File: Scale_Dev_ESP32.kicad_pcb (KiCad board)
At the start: 2 copper layers, 71 parts, among them CON1 USB_B_Micro, CON2 USB_B_Micro, IC1 MCP73831, J1 BUTTON, J2 Jack-DC, M1 ESP-WROOM-32, P1 LIPO, Q1 IRLML5203, Q2 S8050, Q3 S8050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

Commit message: place pcb items
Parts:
- added TP1: TestPoint, TestPoint:TestPoint_Pad_D4.0mm, B.Cu at (144.8, 48.3)
- added TP2: TestPoint, TestPoint:TestPoint_Pad_D4.0mm, B.Cu at (133.3, 48.3)
- added TP3: TestPoint, TestPoint:TestPoint_Pad_D4.0mm, B.Cu at (144.8, 58.4)
- added TP4: TestPoint, TestPoint:TestPoint_Pad_D4.0mm, B.Cu at (133.3, 58.4)
- C15: value CP -> 10uF
- C17: footprint Capacitor_SMD:CP_Elec_4x3 -> Capacitor_Tantalum_SMD:CP_EIA-1608-10_AVX-L_Pad1.25x1.05mm_HandSolder
- C18: footprint Capacitor_SMD:CP_Elec_4x3 -> Capacitor_Tantalum_SMD:CP_EIA-3528-12_Kemet-T_Pad1.50x2.35mm_HandSolder
- U1: footprint Package_DFN_QFN:QFN-24-1EP_4x4mm_P0.5mm_EP2.7x2.7mm_ThermalVias -> Scale:QFN-24-1EP_4x4mm_Pitch0.5mm
- moved J1 119.7 mm to (161.3, 57.1)
- moved CON2 109.7 mm to (154.9, 118.1)
- moved U8 107.5 mm to (163.8, 116.8)
- moved U6 94.6 mm to (118.1, 116.8)
- moved C4 92.7 mm to (136.9, 105.4)
- moved R10 86.4 mm to (143.5, 100.6), turned to 270 degrees
- moved D3 84.5 mm to (132.5, 105.4), turned to 180 degrees
- moved R8 84.4 mm to (139.7, 101.6)
- moved R3 84.0 mm to (128.3, 104.1), turned to 90 degrees
- moved C2 83.4 mm to (124.2, 100.3)
- moved R9 83.4 mm to (139.7, 99.1)
- moved R6 83.2 mm to (134.6, 101.6), turned to 180 degrees
- moved R5 82.5 mm to (134.6, 99.1)
- moved R12 80.4 mm to (143.5, 96.5), turned to 270 degrees
- moved C5 78.3 mm to (128.3, 95.2), turned to 90 degrees
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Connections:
- CON1 pad 4: (no net) -> Net-(CON1-Pad4)
- CON2 pad 4: (no net) -> Net-(CON2-Pad4)
- D5 pad 5: (no net) -> Net-(D5-Pad5)
- D5 pad 6: (no net) -> Net-(D5-Pad6)
- M1 pad 10: (no net) -> /IO25
- M1 pad 11: (no net) -> /IO26
- M1 pad 12: (no net) -> /BUT1
- M1 pad 13: (no net) -> /IO14
- M1 pad 14: (no net) -> /BUT0
- M1 pad 16: /BUT3 -> /IO13
- M1 pad 17: (no net) -> /SD2
- M1 pad 18: (no net) -> /SD3
- M1 pad 19: (no net) -> /CMD
- M1 pad 20: (no net) -> /CLK
- M1 pad 21: (no net) -> /SD0
- M1 pad 22: (no net) -> /SD1
- M1 pad 23: /BUT0 -> /IO15
- M1 pad 24: /BUT1 -> /BUT3
- M1 pad 27: (no net) -> /U2RX
- M1 pad 30: (no net) -> /IO18
- M1 pad 31: (no net) -> /IO19
- M1 pad 32: (no net) -> Net-(M1-Pad32)
- M1 pad 33: (no net) -> /IO21
- M1 pad 37: (no net) -> /IO23
- M1 pad 4: (no net) -> /SENSOR_VP
- M1 pad 5: (no net) -> /SENSOR_VN
- M1 pad 6: (no net) -> /IO34
- M1 pad 7: (no net) -> /IO35
- R10 pad 1: (no net) -> /IO13
- R12 pad 1: (no net) -> /IO15
- R25 pad 1: (no net) -> /U2_RX
- U1 pad 1: (no net) -> Net-(U1-Pad1)
- U1 pad 10: (no net) -> Net-(U1-Pad10)
- U1 pad 11: (no net) -> Net-(U1-Pad11)
- U1 pad 12: (no net) -> Net-(U1-Pad12)
- U1 pad 13: (no net) -> Net-(U1-Pad13)
- U1 pad 14: (no net) -> Net-(U1-Pad14)
- U1 pad 15: (no net) -> Net-(U1-Pad15)
- U1 pad 18: (no net) -> Net-(U1-Pad18)
- U1 pad 19: (no net) -> Net-(U1-Pad19)
- U1 pad 22: (no net) -> Net-(U1-Pad22)
- U1 pad 23: (no net) -> Net-(U1-Pad23)
- U1 pad 24: (no net) -> Net-(U1-Pad24)
- U1 pad 3: (no net) -> /USD_P
- U4 pad 4: (no net) -> Net-(U4-Pad4)
- U5 pad 1: (no net) -> Net-(U5-Pad1)
- U5 pad 10: (no net) -> Net-(U5-Pad10)
- U5 pad 11: (no net) -> Net-(U5-Pad11)
- U5 pad 12: (no net) -> Net-(U5-Pad12)
- U5 pad 13: (no net) -> Net-(U5-Pad13)
- U5 pad 14: (no net) -> Net-(U5-Pad14)
- U5 pad 15: (no net) -> Net-(U5-Pad15)
- U5 pad 16: (no net) -> Net-(U5-Pad16)
- U5 pad 17: (no net) -> Net-(U5-Pad17)
- U5 pad 18: (no net) -> Net-(U5-Pad18)
- U5 pad 2: (no net) -> Net-(U5-Pad2)
- U5 pad 20: (no net) -> Net-(U5-Pad20)
- U5 pad 21: (no net) -> Net-(U5-Pad21)
- U5 pad 22: (no net) -> Net-(U5-Pad22)
- U5 pad 27: (no net) -> Net-(U5-Pad27)
- U5 pad 9: (no net) -> Net-(U5-Pad9)
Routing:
- net GND: track 0.00 -> 55.2 mm
- net +5V: track 0.00 -> 29.8 mm
- net VCC: track 0.00 -> 26.9 mm
- net +BATT: track 0.00 -> 8.73 mm
- net +3V3: track 0.00 -> 7.26 mm
- net Net-(C4-Pad2): track 0.00 -> 5.74 mm
- net Net-(CON1-Pad1): track 0.00 -> 4.35 mm
- net Net-(R17-Pad1): track 0.00 -> 1.76 mm
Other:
- board outline added: 53.3 x 77.5 mm
- net class Default: trace_width 0.25 -> 0.3; via_dia 0.8 -> 1; via_drill 0.4 -> 0.6
- net class POWER added: clearance 0.2, trace_width 0.5, via_dia 1, via_drill 0.6

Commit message: update pcb wire
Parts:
- CON1, CON2: footprint Connectors_USB:USB_Micro-B_Molex-105017-0001 -> Connectors_USB:USB_Micro-B_Molex_47346-0001
- moved D5 1.27 mm to (154.8, 104.6), turned to 180 degrees
- moved CON1 0.97 mm to (140.4, 118.8)
- moved CON2 0.72 mm to (154.8, 118.8)
- turned C6 to 180 degrees
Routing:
- net GND: track 55.2 -> 302.6 mm, vias 0 -> 6
- net +3V3: track 7.26 -> 162.9 mm, vias 0 -> 4
- net VCC: track 26.9 -> 74.5 mm, vias 0 -> 4
- net /EN: track 0.00 -> 25.1 mm
- net +BATT: track 8.73 -> 31.0 mm
- net Net-(IC1-Pad5): track 0.00 -> 14.1 mm
- net /RTS: track 0.00 -> 12.1 mm
- net /IO33: track 0.00 -> 11.1 mm, vias 0 -> 2
- net /IO32: track 0.00 -> 10.4 mm, vias 0 -> 2
- net /DTR: track 0.00 -> 7.78 mm
- net /USB_N: track 0.00 -> 6.87 mm
- net /USB_P: track 0.00 -> 5.48 mm
- net Net-(Q2-Pad1): track 0.00 -> 4.11 mm
- net Net-(D2-Pad1): track 0.00 -> 3.26 mm
- net Net-(CON1-Pad3): track 0.00 -> 3.22 mm
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
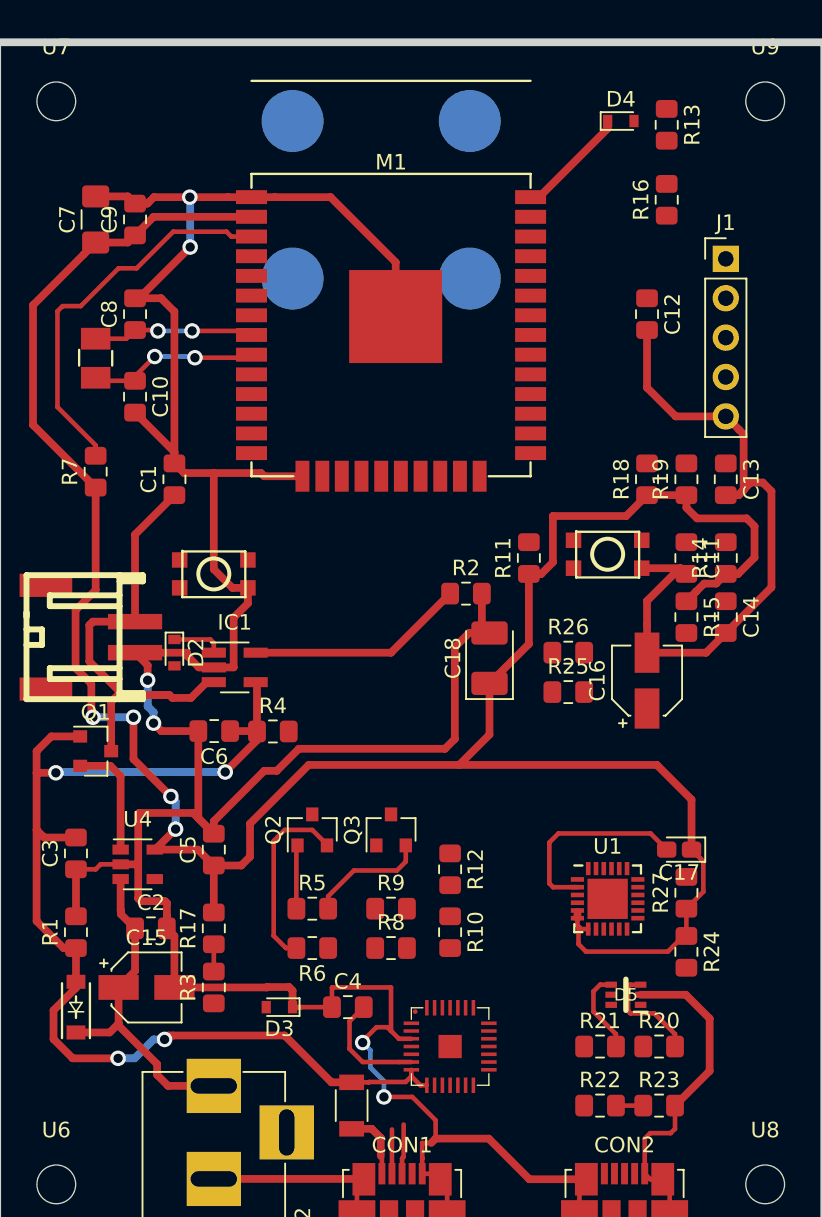
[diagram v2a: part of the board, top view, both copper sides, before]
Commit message: update pcb route
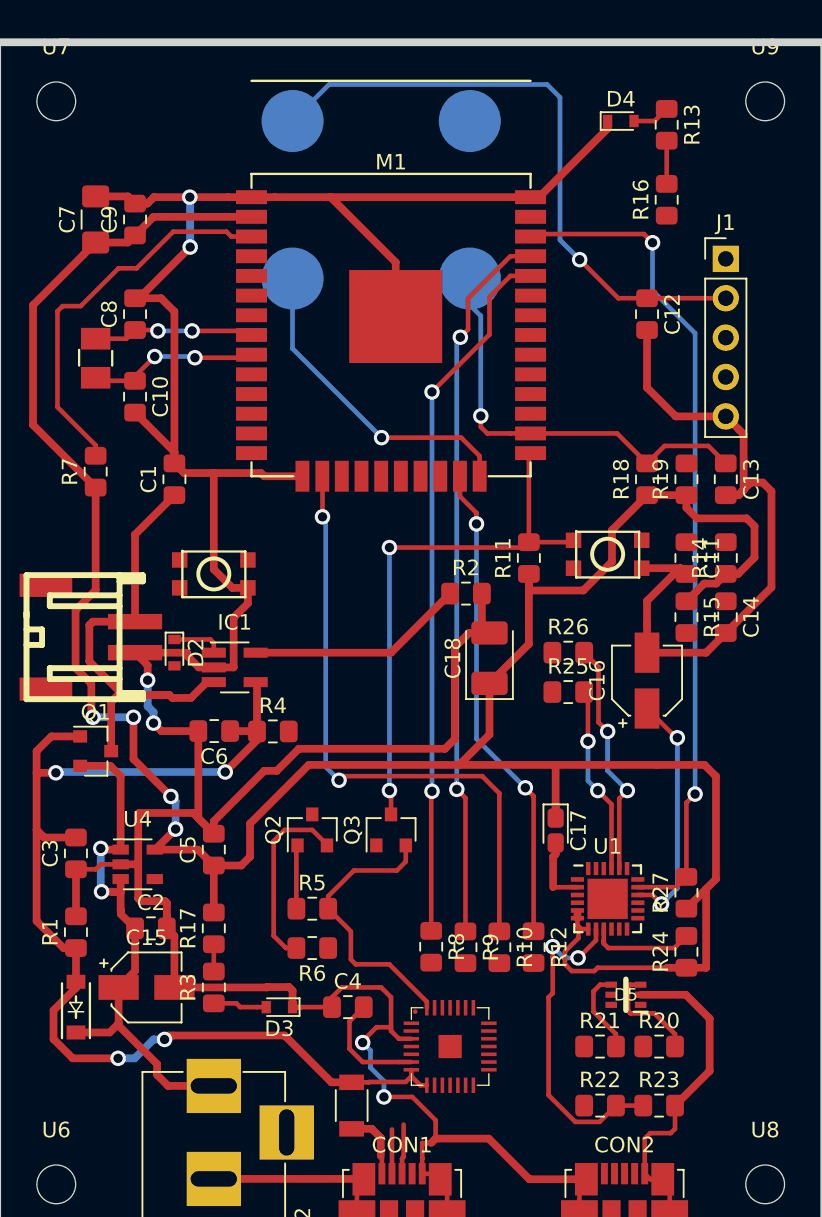
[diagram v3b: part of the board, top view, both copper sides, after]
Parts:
- moved C17 8.06 mm to (150.3, 94.0), turned to 270 degrees
- moved R12 7.36 mm to (148.9, 101.5)
- moved R9 5.41 mm to (144.5, 101.5), turned to 270 degrees
- moved R10 3.32 mm to (146.7, 101.5)
- moved R8 2.59 mm to (142.3, 101.5), turned to 270 degrees
- turned R24 to 90 degrees
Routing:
- net /CP2110_SUS: track 0.00 -> 53.8 mm, vias 0 -> 2
- net /TXD0: track 0.00 -> 46.5 mm, vias 0 -> 2
- net /RXD0: track 0.00 -> 45.7 mm, vias 0 -> 2
- net /BUT1: track 0.00 -> 40.0 mm, vias 0 -> 1
- net /IO13: track 0.00 -> 39.9 mm, vias 0 -> 2
- net /IO0: track 0.00 -> 35.1 mm, vias 0 -> 2
- net /IO15: track 0.00 -> 31.3 mm, vias 0 -> 2
- net /BUT2: track 0.00 -> 27.6 mm, vias 0 -> 1
- net /BUT3: track 0.00 -> 20.8 mm, vias 0 -> 1
- net /VBUS: track 1.76 -> 21.2 mm, vias 0 -> 2
- net Net-(C16-Pad1): track 0.00 -> 15.6 mm, vias 0 -> 2
- net Net-(R26-Pad2): track 0.00 -> 15.3 mm, vias 0 -> 2
- net +3V3: track 162.9 -> 176.5 mm
- net Net-(R25-Pad2): track 0.00 -> 12.1 mm, vias 0 -> 2
- net /DTR: track 7.78 -> 18.1 mm
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
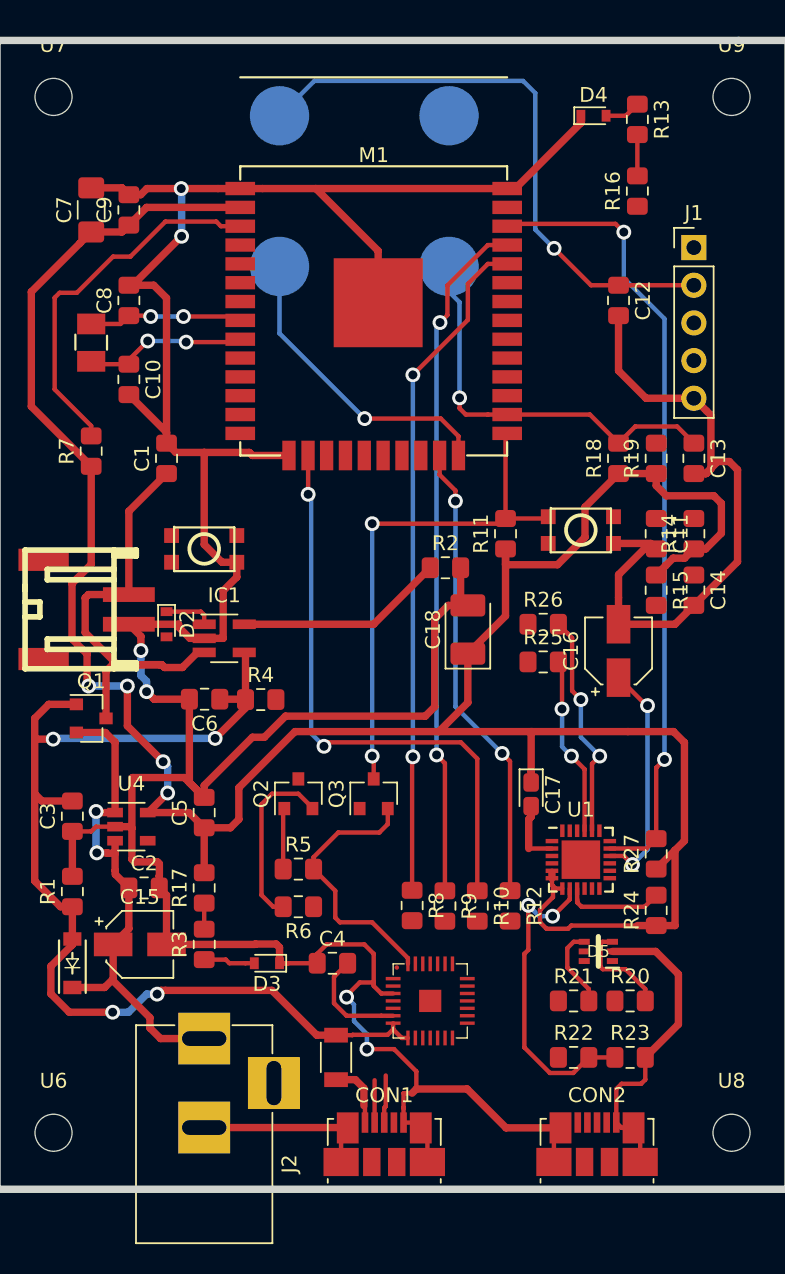
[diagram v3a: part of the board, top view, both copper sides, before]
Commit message: update pcb route
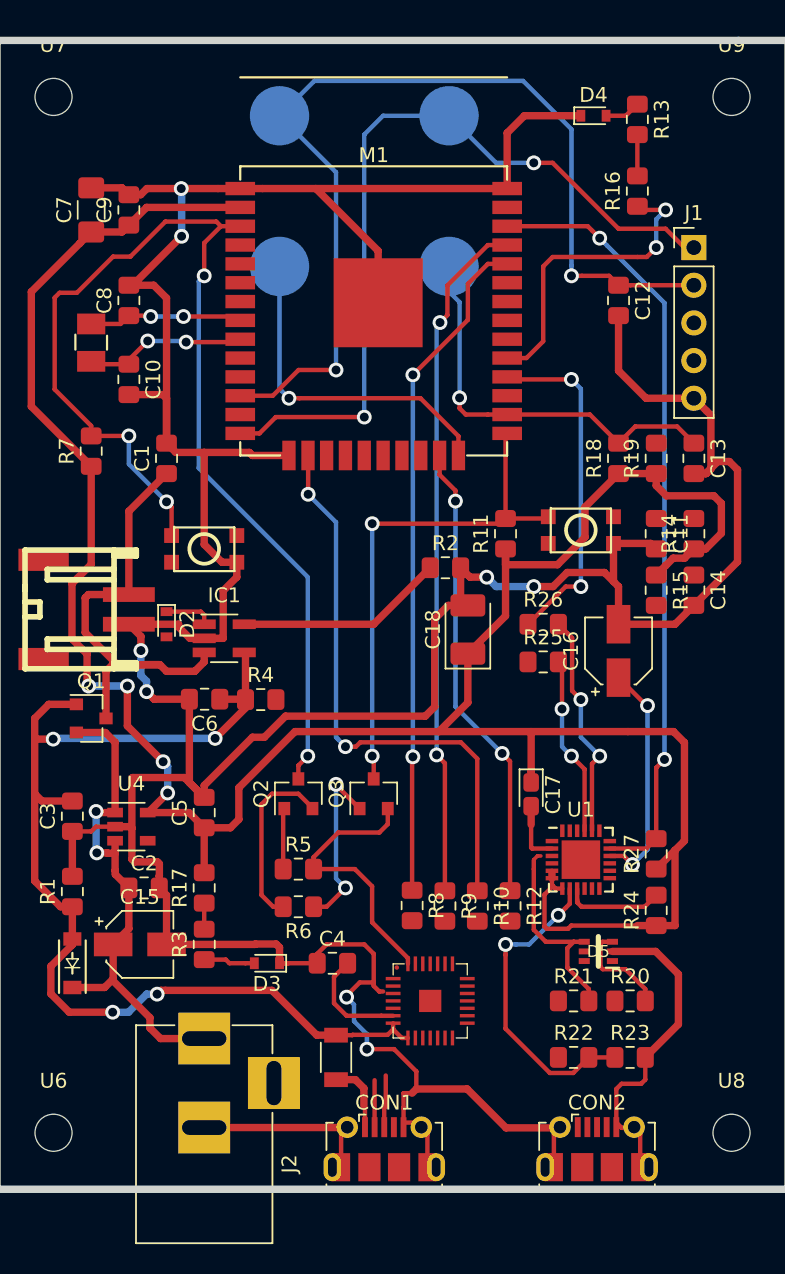
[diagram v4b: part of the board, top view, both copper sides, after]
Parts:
- CON1, CON2: footprint Connectors_USB:USB_Micro-B_Molex_47346-0001 -> Connectors_USB:USB_Micro-B_Molex-105017-0001
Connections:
- U1 pad 3: /USD_P -> /USB_P
- U5 pad 26: Net-(R8-Pad2) -> (no net)
- U5 pad 27: Net-(U5-Pad27) -> (no net)
- U5 pad 28: /DTR -> (no net)
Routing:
- net /BUT0: track 0.00 -> 54.3 mm, vias 0 -> 2
- net /EN: track 25.1 -> 76.8 mm, vias 0 -> 4
- net /BUT1: track 40.0 -> 66.3 mm, vias 1 -> 2
- net /U2_TX: track 0.00 -> 23.3 mm, vias 0 -> 2
- net /IO5: track 0.00 -> 20.9 mm, vias 0 -> 2
- net GND: track 306.4 -> 319.1 mm, vias 6 -> 8
- net Net-(Q3-Pad1): track 0.00 -> 12.2 mm, vias 0 -> 2
- net /USB_P: track 5.48 -> 13.8 mm
- net /BUT3: track 20.8 -> 22.9 mm
- net /CP2110_SUS: track 53.8 -> 52.5 mm
- net /IO13: track 39.9 -> 39.1 mm
- net +BATT: track 31.0 -> 31.6 mm

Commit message: update route from linux machine
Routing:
- net /BUT1: track 66.3 -> 98.2 mm, vias 2 -> 4
- net Net-(CON2-Pad1): track 0.00 -> 27.0 mm, vias 0 -> 4
- net Net-(D2-Pad2): track 0.00 -> 13.4 mm, vias 0 -> 2
- net Net-(CON2-Pad3): track 0.00 -> 13.2 mm, vias 0 -> 2
- net /BUT2: track 27.6 -> 38.2 mm, vias 1 -> 3
- net /BUT3: track 22.9 -> 33.1 mm, vias 1 -> 3
- net Net-(CON2-Pad2): track 0.00 -> 9.62 mm, vias 0 -> 2
- net /VBUS: track 21.2 -> 23.9 mm
- net GND: track 319.1 -> 321.5 mm
- net /USB_P: track 13.8 -> 14.6 mm
- net +BATT: track 31.6 -> 32.1 mm

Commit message: update route ubuntu
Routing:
- net GND: track 321.5 -> 374.2 mm, vias 8 -> 9
- net /BUT3: track 33.1 -> 67.4 mm, vias 3 -> 5
- net /BUT0: track 54.3 -> 86.5 mm, vias 2 -> 4
- net /RTS: track 12.1 -> 31.9 mm, vias 0 -> 2
- net Net-(CON1-Pad3): track 3.22 -> 17.4 mm, vias 0 -> 2
- net /USB_N: track 6.87 -> 16.2 mm
- net Net-(CON1-Pad2): track 2.86 -> 11.8 mm, vias 0 -> 2
- net Net-(R12-Pad2): track 0.00 -> 6.15 mm
- net Net-(R9-Pad2): track 0.00 -> 3.29 mm
- net +3V3: track 176.3 -> 175.0 mm
- net Net-(C4-Pad2): track 7.41 -> 8.20 mm
- net /DTR: track 18.4 -> 18.9 mm
